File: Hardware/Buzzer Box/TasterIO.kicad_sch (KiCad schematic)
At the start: 4 parts, among them J3 Conn_01x03_Socket, Q1 AO3400A, U3 LTV-817S

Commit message: Updated the PCB
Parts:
- removed J3: Conn_01x03_Socket, Connector_JST:JST_XH_B3B-XH-AM_1x03_P2.50mm_Vertical, symbol Connector:Conn_01x03_Socket
- added J13: NC3FAAH, Connector_Audio:Jack_XLR_Neutrik_NC3FAAH_Horizontal, symbol Connector_Audio:NC3FAAH
- R3: footprint Resistor_SMD:R_0805_2012Metric -> Resistor_SMD:R_0603_1608Metric
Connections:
- net +24V: now also J13.1
- net at Q1.3 (D): now also J13.3
- net at R3.1: now also J13.2
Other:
- moved on the sheet: Q1, R3, U3

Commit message: made chages to the PCB
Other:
- company: (none) -> EinfachTechnik
- title: (none) -> BuzzerPCB
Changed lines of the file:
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@@
 	(generator_version "8.0")
 	(paper "A4")
+	(title_block
+		(title "BuzzerPCB")
+		(date "2024-12-23")
+		(rev "2")
+		(company "EinfachTechnik")
+	)
 	(wire
 		(pts

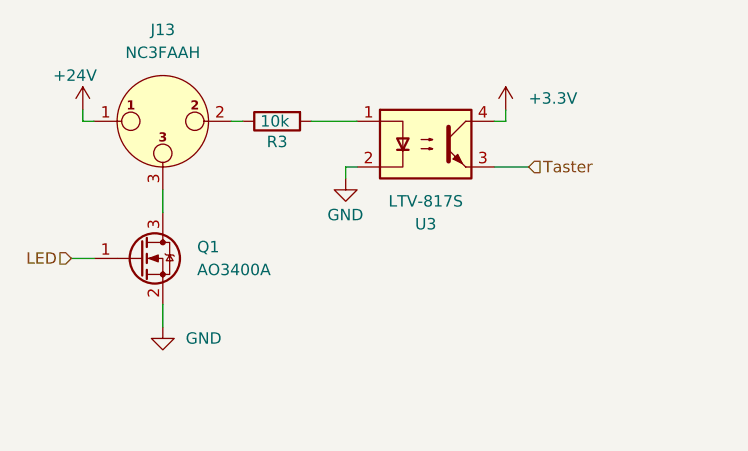
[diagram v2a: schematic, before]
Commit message: added debouncing caps
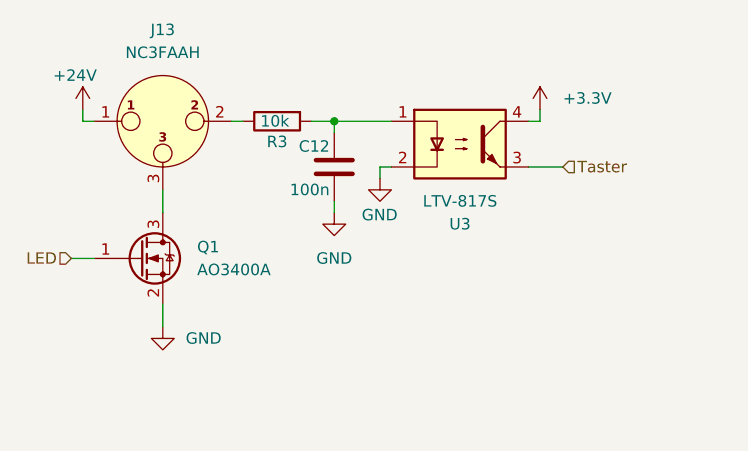
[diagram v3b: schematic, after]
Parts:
- added C12: 100n, Capacitor_SMD:C_0603_1608Metric, symbol Device:C
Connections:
- net GND: now also C12.1
- net at R3.2, U3.1: now also C12.2
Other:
- moved on the sheet: U3

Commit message: some changes
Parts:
- J13: footprint Connector_Audio:Jack_XLR_Neutrik_NC3FAAH_Horizontal -> Felix_XLR:Jack_XLR_Neutrik_NC3FAAH_Horizontal
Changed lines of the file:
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@@
 			)
 		)
-		(property "Footprint" "Connector_Audio:Jack_XLR_Neutrik_NC3FAAH_Horizontal"
+		(property "Footprint" "Felix_XLR:Jack_XLR_Neutrik_NC3FAAH_Horizontal"
 			(at 76.2 68.58 0)
 			(effects
